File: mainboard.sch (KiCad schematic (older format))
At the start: 37 parts, among them J1 To battery holder, J2 To RED display, J3 To GREEN display, J4 To BLUE display, Q1 PNP S8550, Q2 NPN 2N5551, SW1 GREEN, SW2 STOP, SW3 START, SW4 RED, SW5 BLUE, U1 LM555xN, U2 CD4015 for RED, U3 CD4015 for GREEN, U4 CD4015 for BLUE

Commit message: fix symbol according to pinout from datasheets
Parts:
- Q1: symbol Device:Q_PNP_BCE -> Device:Q_PNP_EBC
- Q2: symbol Device:Q_NPN_BCE -> Device:Q_NPN_CBE
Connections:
- net GND_MAIN: now also Q2.1 (C); no longer Q2.2 (C)
- net VCC: now also Q1.1 (E); no longer Q1.3 (E)
- net at R5.1, R6.2: now also Q1.2 (B); no longer Q1.1 (B)
- net at R7.2: now also Q1.3 (C); no longer Q1.2 (C)
- net at R7.1, SW2.1: now also Q2.2 (B); no longer Q2.1 (B)
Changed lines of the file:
@@
 $EndComp
 $Comp
-L Device:Q_PNP_BCE Q1
+L Device:Q_PNP_EBC Q1
 U 1 1 62287DCD
 P 2400 2500
@@
 $EndComp
 $Comp
-L Device:Q_NPN_BCE Q2
+L Device:Q_NPN_CBE Q2
 U 1 1 6228999F
 P 3100 3000

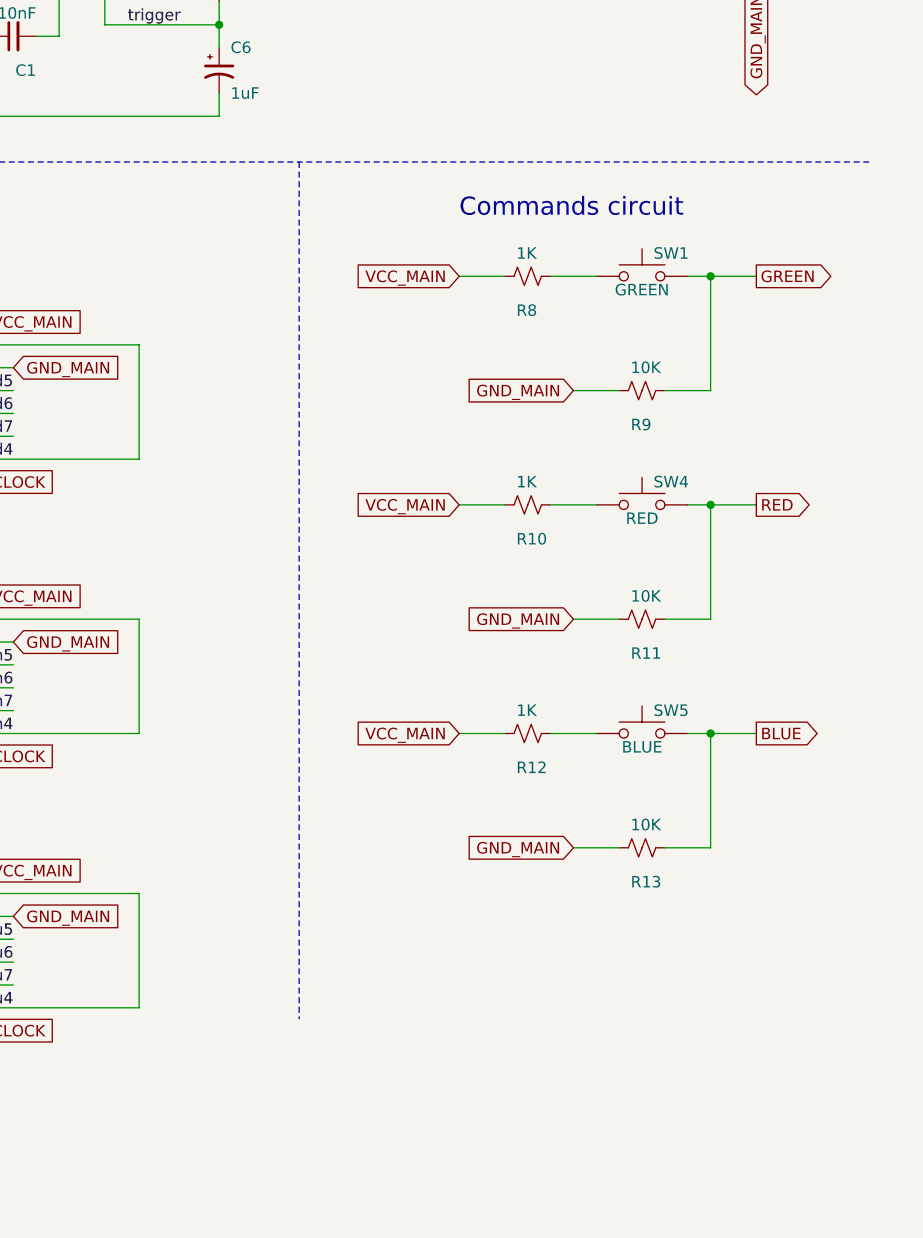
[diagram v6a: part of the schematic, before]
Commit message: added mounting holes
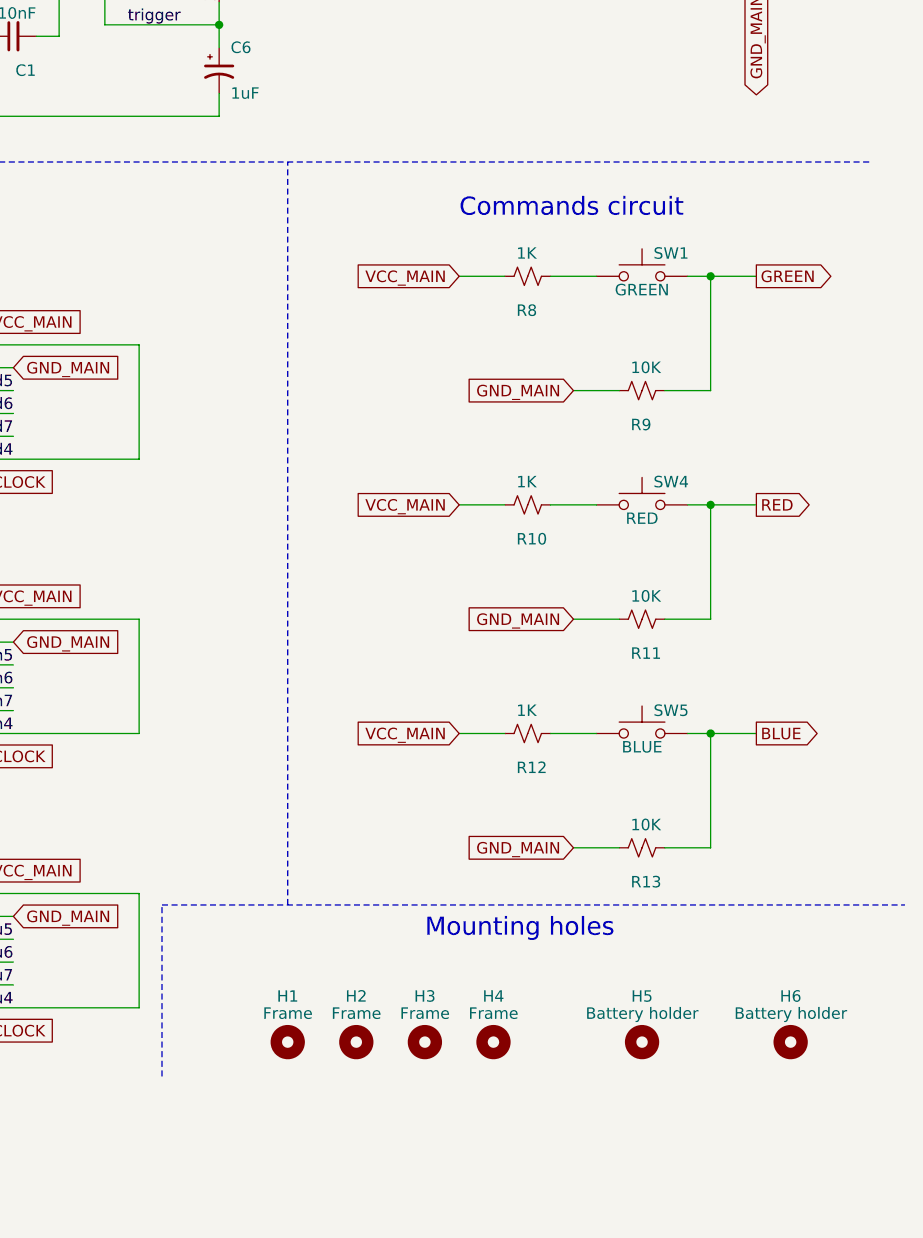
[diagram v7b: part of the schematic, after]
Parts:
- added H1, H2, H3, H4: Frame, MountingHole:MountingHole_3.2mm_M3_DIN965_Pad, symbol Mechanical:MountingHole
- added H5, H6: Battery holder, MountingHole:MountingHole_3.2mm_M3_DIN965_Pad, symbol Mechanical:MountingHole
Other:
- note added: "Mounting holes"
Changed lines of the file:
@@
 Wire Notes Line
 	650  4000 4500 4000
-Wire Notes Line
-	8500 2500 8500 6250
 $Comp
 L Device:C_Small C2
@@
 	8150 2300 6750 2300
 Connection ~ 6750 2300
+$Comp
+L Mechanical:MountingHole H2
+U 1 1 624A57EA
+P 8750 6350
+F 0 "H2" H 8750 6550 50  0000 C CNN
+F 1 "Frame" H 8750 6475 50  0000 C CNN
+F 2 "MountingHole:MountingHole_3.2mm_M3_DIN965_Pad" H 8750 6350 50  0001 C CNN
+F 3 "~" H 8750 6350 50  0001 C CNN
+	1    8750 6350
+	1    0    0    -1
+$EndComp
+$Comp
+L Mechanical:MountingHole H3
+U 1 1 624A5A1B
+P 9050 6350
+F 0 "H3" H 9050 6550 50  0000 C CNN
+F 1 "Frame" H 9050 6475 50  0000 C CNN
+F 2 "MountingHole:MountingHole_3.2mm_M3_DIN965_Pad" H 9050 6350 50  0001 C CNN
+F 3 "~" H 9050 6350 50  0001 C CNN
+	1    9050 6350
+	1    0    0    -1
+$EndComp
+$Comp
+L Mechanical:MountingHole H4
+U 1 1 624A5C60
+P 9350 6350
+F 0 "H4" H 9350 6550 50  0000 C CNN
+F 1 "Frame" H 9350 6475 50  0000 C CNN
+F 2 "MountingHole:MountingHole_3.2mm_M3_DIN965_Pad" H 9350 6350 50  0001 C CNN
+F 3 "~" H 9350 6350 50  0001 C CNN
+	1    9350 6350
+	1    0    0    -1
+$EndComp
+$Comp
+L Mechanical:MountingHole H5
+U 1 1 624A5F47
+P 10000 6350
+F 0 "H5" H 10000 6550 50  0000 C CNN
+F 1 "Battery holder" H 10000 6475 50  0000 C CNN
+F 2 "MountingHole:MountingHole_3.2mm_M3_DIN965_Pad" H 10000 6350 50  0001 C CNN
+F 3 "~" H 10000 6350 50  0001 C CNN
+	1    10000 6350
+	1    0    0    -1
+$EndComp
+$Comp
+L Mechanical:MountingHole H6
+U 1 1 624A629B
+P 10650 6350
+F 0 "H6" H 10650 6550 50  0000 C CNN
+F 1 "Battery holder" H 10650 6475 50  0000 C CNN
+F 2 "MountingHole:MountingHole_3.2mm_M3_DIN965_Pad" H 10650 6350 50  0001 C CNN
+F 3 "~" H 10650 6350 50  0001 C CNN
+	1    10650 6350
+	1    0    0    -1
+$EndComp
+$Comp
+L Mechanical:MountingHole H1
+U 1 1 624A65F8
+P 8450 6350
+F 0 "H1" H 8450 6550 50  0000 C CNN
+F 1 "Frame" H 8450 6475 50  0000 C CNN
+F 2 "MountingHole:MountingHole_3.2mm_M3_DIN965_Pad" H 8450 6350 50  0001 C CNN
+F 3 "~" H 8450 6350 50  0001 C CNN
+	1    8450 6350
+	1    0    0    -1
+$EndComp
+Wire Notes Line
+	7900 6500 7900 5750
+Wire Notes Line
+	7900 5750 11150 5750
+Wire Notes Line
+	8450 5750 8450 2500
+Text Notes 9050 5900 0    79   ~ 0
+Mounting holes
 $EndSCHEMATC
